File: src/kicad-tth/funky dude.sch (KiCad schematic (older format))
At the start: 30 parts, among them P1 CONN_2, P2 CONN_2, P3 CONN_2, U1 OP284

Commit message: 2014-10-23.2 - PCB is routed
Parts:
- C13: footprint Custom:C2-LARGE_PADS -> (none)
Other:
- moved on the sheet: C1, C10, C12, C13, C2, C3, C4, C5, C6, C7, C8, C9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

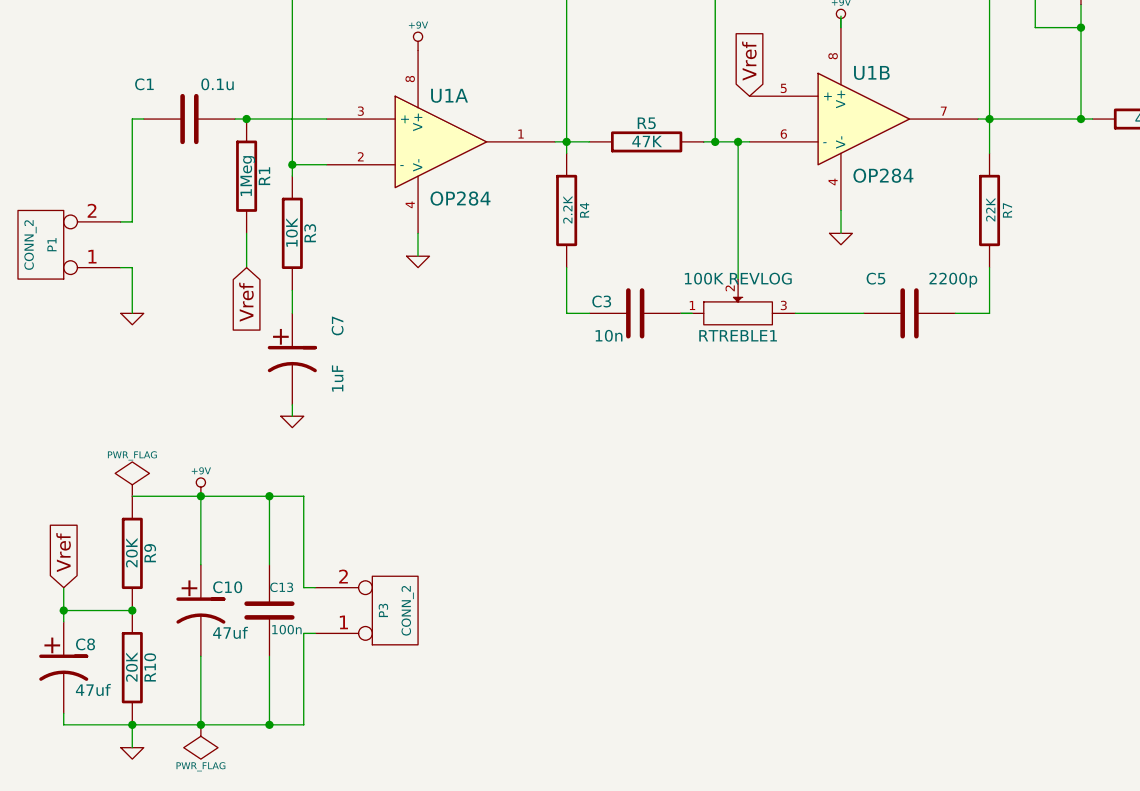
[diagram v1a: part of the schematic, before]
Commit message: change to TLC2262
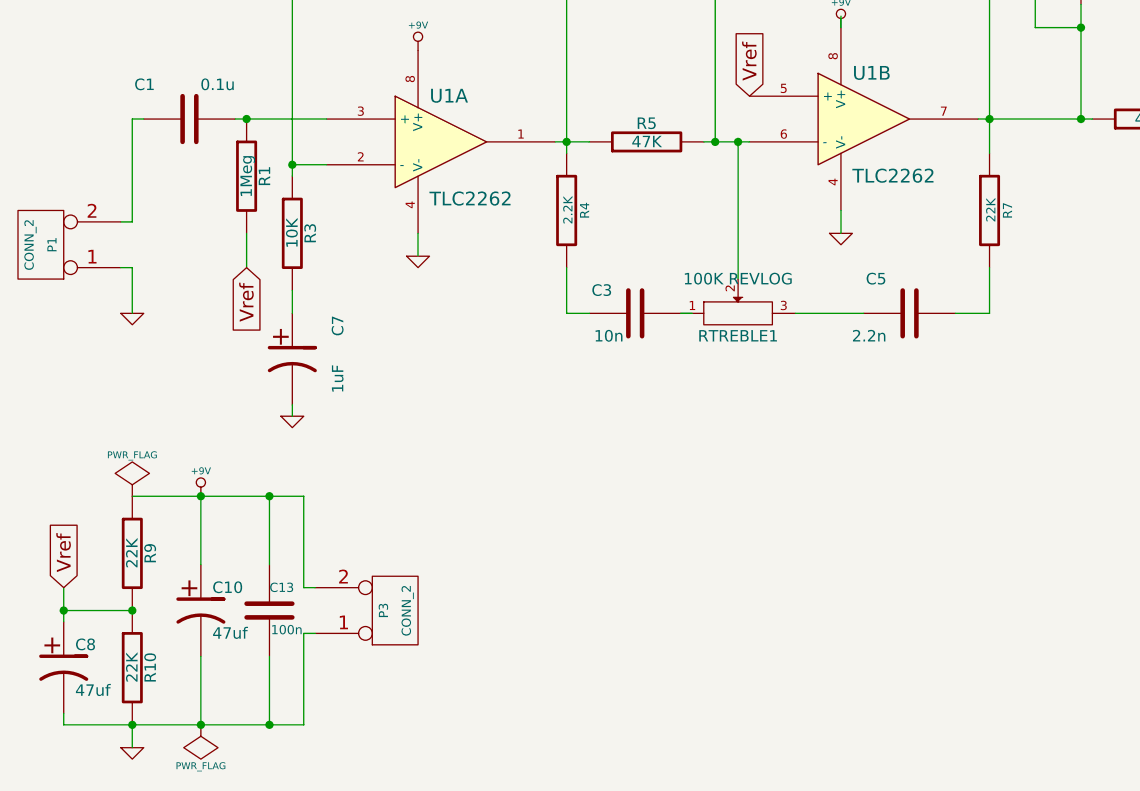
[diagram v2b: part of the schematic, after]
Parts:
- C5: value 2200p -> 2.2n
- R10, R9: value 20K -> 22K
- U1: value OP284 -> TLC2262
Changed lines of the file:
@@
 P 5250 7300
 F 0 "R10" V 5330 7300 50  0000 C CNN
-F 1 "20K" V 5250 7300 50  0000 C CNN
+F 1 "22K" V 5250 7300 50  0000 C CNN
 F 2 "Custom:R3-LARGE_PADS" H 5250 7300 60  0001 C CNN
 F 3 "" H 5250 7300 60  0001 C CNN
@@
 P 5250 6800
 F 0 "R9" V 5330 6800 50  0000 C CNN
-F 1 "20K" V 5250 6800 50  0000 C CNN
+F 1 "22K" V 5250 6800 50  0000 C CNN
 F 2 "Custom:R3-LARGE_PADS" H 5250 6800 60  0001 C CNN
 F 3 "" H 5250 6800 60  0001 C CNN
@@
 P 8650 5750
 F 0 "C5" V 8800 5850 50  0000 L CNN
-F 1 "2200p" V 8800 5450 50  0000 L CNN
+F 1 "2.2n" V 8550 5850 50  0000 L CNN
 F 2 "Custom:C2-LARGE_PADS" H 8650 5750 60  0001 C CNN
 F 3 "" H 8650 5750 60  0001 C CNN
@@
 U 1 1 5194A4FE
 P 7450 5750
-F 0 "C3" V 7500 5850 50  0000 L CNN
+F 0 "C3" V 7550 5850 50  0000 L CNN
 F 1 "10n" V 7350 5800 50  0000 L CNN
 F 2 "Custom:C2-LARGE_PADS" H 7450 5750 60  0001 C CNN
@@
 P 8450 4900
 F 0 "U1" H 8400 5100 60  0000 L CNN
-F 1 "OP284" H 8400 4650 60  0000 L CNN
+F 1 "TLC2262" H 8400 4650 60  0000 L CNN
 F 2 "Custom:DIP-8_LARGE_PADS" H 8450 4900 60  0001 C CNN
 F 3 "" H 8450 4900 60  0000 C CNN
@@
 P 6600 5000
 F 0 "U1" H 6550 5200 60  0000 L CNN
-F 1 "OP284" H 6550 4750 60  0000 L CNN
+F 1 "TLC2262" H 6550 4750 60  0000 L CNN
 F 2 "Custom:DIP-8_LARGE_PADS" H 6600 5000 60  0001 C CNN
 F 3 "" H 6600 5000 60  0000 C CNN

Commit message: pcb changes
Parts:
- C13: footprint (none) -> Custom:C2-LARGE_PADS
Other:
- moved on the sheet: C3
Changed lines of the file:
@@
 Wire Wire Line
 	7800 3500 7800 3400
-Wire Wire Line
-	7650 5750 7700 5750
 Connection ~ 9000 4100
 Connection ~ 9000 4900
 Wire Wire Line
 	9000 3950 9000 5050
-Wire Wire Line
-	7150 5750 7250 5750
 Connection ~ 7800 4100
 Wire Wire Line
@@
 L C C3
 U 1 1 5194A4FE
-P 7450 5750
-F 0 "C3" V 7550 5850 50  0000 L CNN
-F 1 "10n" V 7350 5800 50  0000 L CNN
-F 2 "Custom:C2-LARGE_PADS" H 7450 5750 60  0001 C CNN
-F 3 "" H 7450 5750 60  0001 C CNN
-	1    7450 5750
+P 7400 5750
+F 0 "C3" V 7500 5850 50  0000 L CNN
+F 1 "10n" V 7300 5800 50  0000 L CNN
+F 2 "Custom:C2-LARGE_PADS" H 7400 5750 60  0001 C CNN
+F 3 "" H 7400 5750 60  0001 C CNN
+	1    7400 5750
 	0    -1   -1   0
 $EndComp
@@
 F 0 "C13" H 5850 7150 40  0000 L CNN
 F 1 "100n" H 5856 6965 40  0000 L CNN
-F 2 "" H 5888 6900 30  0000 C CNN
+F 2 "Custom:C2-LARGE_PADS" H 5888 6900 30  0001 C CNN
 F 3 "~" H 5850 7050 60  0000 C CNN
 	1    5850 7050
@@
 	9200 4500 9400 4500
 Connection ~ 9400 4500
+Wire Wire Line
+	7150 5750 7200 5750
+Wire Wire Line
+	7650 5750 7600 5750
 $EndSCHEMATC

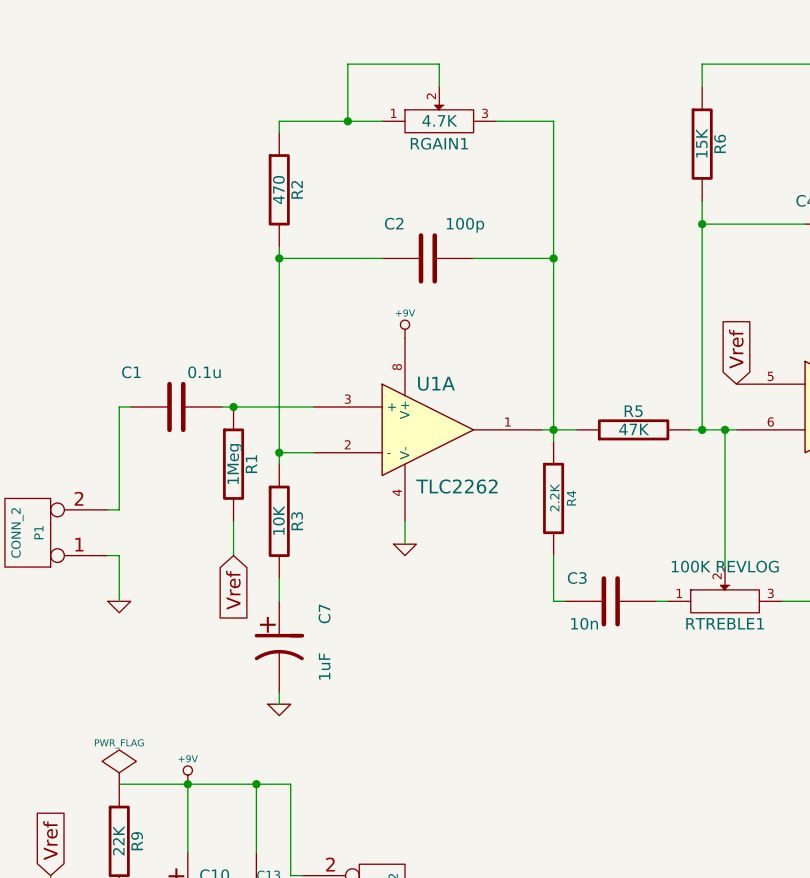
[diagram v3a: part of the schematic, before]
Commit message: smaller bcb design, removed gain trim
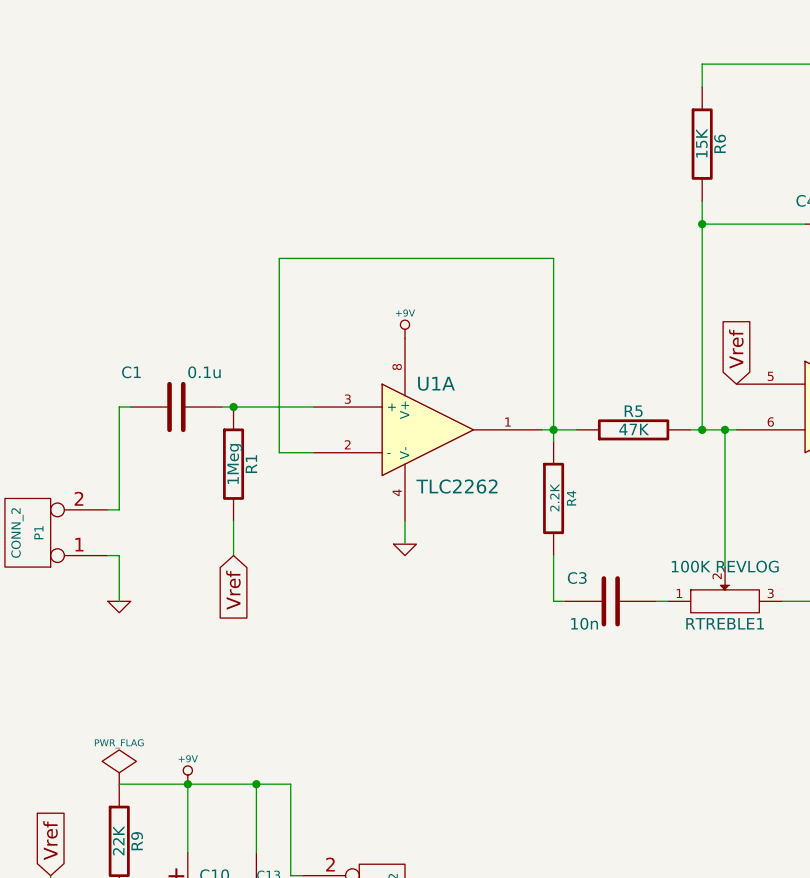
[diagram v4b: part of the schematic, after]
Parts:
- removed C2: 100p, Custom:C2-LARGE_PADS, symbol C
- removed C7: 1uF, Custom:C1V5-LARGE_PADS, symbol CP1
- removed R2: 470, Custom:R3-LARGE_PADS, symbol R
- removed R3: 10K, Custom:R3-LARGE_PADS, symbol R
- removed RGAIN1: 4.7K, Discret:RV2, symbol POT
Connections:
- net at R4.1, R5.1, U1.1: now also U1.2 (-)
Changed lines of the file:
@@
 	5250 4900 5250 5350
-Wire Wire Line
-	6650 3400 6650 3500
 Wire Wire Line
 	7800 3500 7800 3400
@@
 Vref
 $Comp
-L POT RGAIN1
-U 1 1 5194A7CF
-P 6650 3650
-F 0 "RGAIN1" H 6650 3550 50  0000 C CNN
-F 1 "4.7K" H 6650 3650 50  0000 C CNN
-F 2 "Discret:RV2" H 6650 3650 60  0001 C CNN
-F 3 "" H 6650 3650 60  0001 C CNN
-	1    6650 3650
-	1    0    0    -1
-$EndComp
-$Comp
 L POT RTREBLE1
 U 1 1 5194A643
@@
 	1    0    0    -1
 $EndComp
-$Comp
-L R R3
-U 1 1 51B1A74C
-P 5950 5400
-F 0 "R3" V 6030 5400 50  0000 C CNN
-F 1 "10K" V 5950 5400 50  0000 C CNN
-F 2 "Custom:R3-LARGE_PADS" H 5950 5400 60  0001 C CNN
-F 3 "" H 5950 5400 60  0000 C CNN
-	1    5950 5400
-	1    0    0    -1
-$EndComp
-$Comp
-L R R2
-U 1 1 51B1A765
-P 5950 3950
-F 0 "R2" V 6030 3950 50  0000 C CNN
-F 1 "470" V 5950 3950 50  0000 C CNN
-F 2 "Custom:R3-LARGE_PADS" H 5950 3950 60  0001 C CNN
-F 3 "" H 5950 3950 60  0000 C CNN
-	1    5950 3950
-	1    0    0    -1
-$EndComp
 Wire Wire Line
 	5950 5100 6100 5100
 Wire Wire Line
-	5950 4200 5950 5150
-Wire Wire Line
 	5750 5400 5750 5550
-Wire Wire Line
-	5950 5650 5950 5750
 Text GLabel 5750 5550 3    60   Input ~ 0
 Vref
-$Comp
-L C C2
-U 1 1 51B1A91A
-P 6600 4250
-F 0 "C2" V 6750 4350 50  0000 L CNN
-F 1 "100p" V 6750 4000 50  0000 L CNN
-F 2 "Custom:C2-LARGE_PADS" H 6600 4250 60  0001 C CNN
-F 3 "" H 6600 4250 60  0000 C CNN
-	1    6600 4250
-	0    -1   -1   0
-$EndComp
-Wire Wire Line
-	6400 4250 5950 4250
-Connection ~ 5950 4250
-Wire Wire Line
-	7150 4250 6800 4250
-Wire Wire Line
-	5950 3650 6400 3650
-Wire Wire Line
-	6900 3650 7150 3650
-Connection ~ 7150 4250
+Wire Wire Line
+	5950 4250 7150 4250
 $Comp
 L CONN_2 P3
@@
 Wire Wire Line
 	7800 3400 9500 3400
-Wire Wire Line
-	6650 3400 6250 3400
-Wire Wire Line
-	6250 3400 6250 3650
-Connection ~ 6250 3650
 $Comp
 L R R4
@@
 $EndComp
 Wire Wire Line
-	7150 3650 7150 5050
+	7150 4250 7150 5050
 Wire Wire Line
 	7150 5550 7150 5750
@@
 Wire Wire Line
 	10450 5100 10500 5100
-Connection ~ 5950 5100
 Connection ~ 9400 3400
 Wire Wire Line
 	10450 3400 10550 3400
-$Comp
-L CP1 C7
-U 1 1 5447DDCC
-P 5950 5950
-F 0 "C7" V 6150 6050 50  0000 L CNN
-F 1 "1uF" V 6150 5800 50  0000 L CNN
-F 2 "Custom:C1V5-LARGE_PADS" H 5950 5950 60  0001 C CNN
-F 3 "" H 5950 5950 60  0001 C CNN
-	1    5950 5950
-	1    0    0    -1
-$EndComp
-Wire Wire Line
-	5950 6150 5950 6200
-$Comp
-L GND #PWR012
-U 1 1 5447DFA2
-P 5950 6200
-F 0 "#PWR012" H 5950 6200 30  0001 C CNN
-F 1 "GND" H 5950 6130 30  0001 C CNN
-F 2 "" H 5950 6200 60  0001 C CNN
-F 3 "" H 5950 6200 60  0001 C CNN
-	1    5950 6200
-	1    0    0    -1
-$EndComp
 $Comp
 L R R8
@@
 Wire Wire Line
 	9950 4900 10050 4900
-Wire Wire Line
-	5950 3650 5950 3700
 Connection ~ 7900 5000
 Wire Wire Line
@@
 Wire Wire Line
 	7650 5750 7600 5750
+Wire Wire Line
+	5950 4250 5950 5100
 $EndSCHEMATC
